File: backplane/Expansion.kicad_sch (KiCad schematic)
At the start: 19 parts, among them U401 74HC245, U402 74HC245, U403 74HC245, U404 74HC245, U405 74HC245, U406 74HC245, U407 ATF22V10C

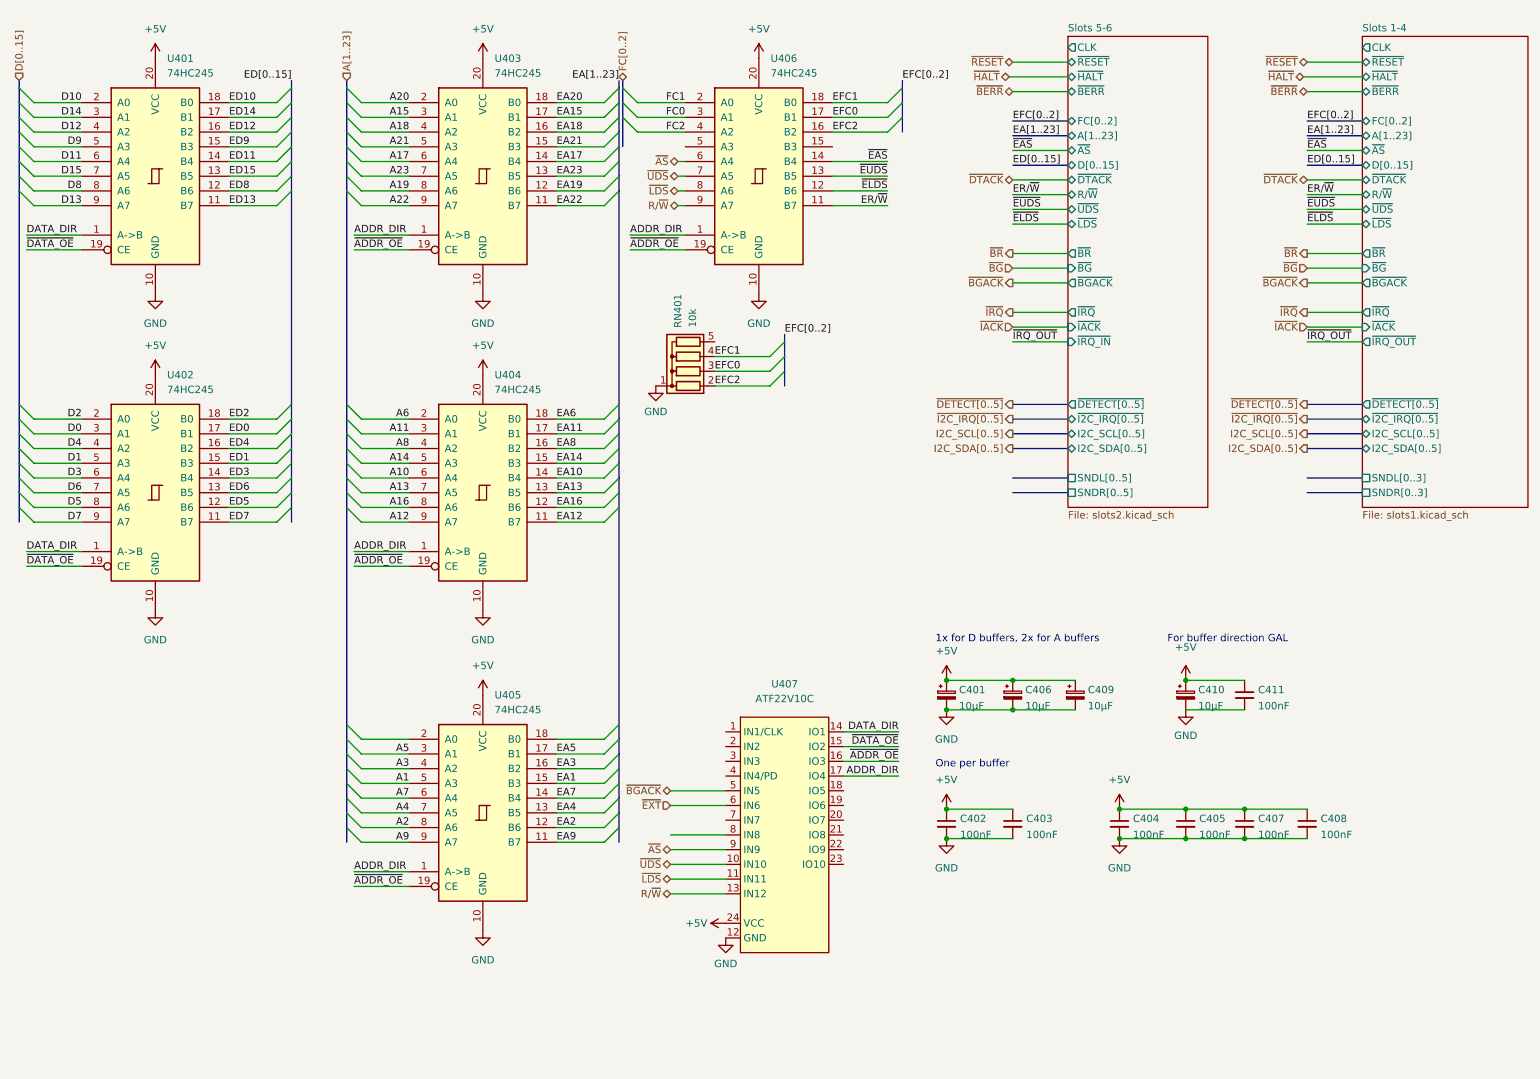
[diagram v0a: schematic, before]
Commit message: More backplane work
- Added pull up/down resistors at end of board to bring the various
  data/address lines to a controlled state, rather than floating, and
  attempt to control reflections

- Added a clock buffer so each slot gets its own nice buffered clock.

  The clock buffer used is only 1:5 fanout, so the last two slots share
  a clock line.
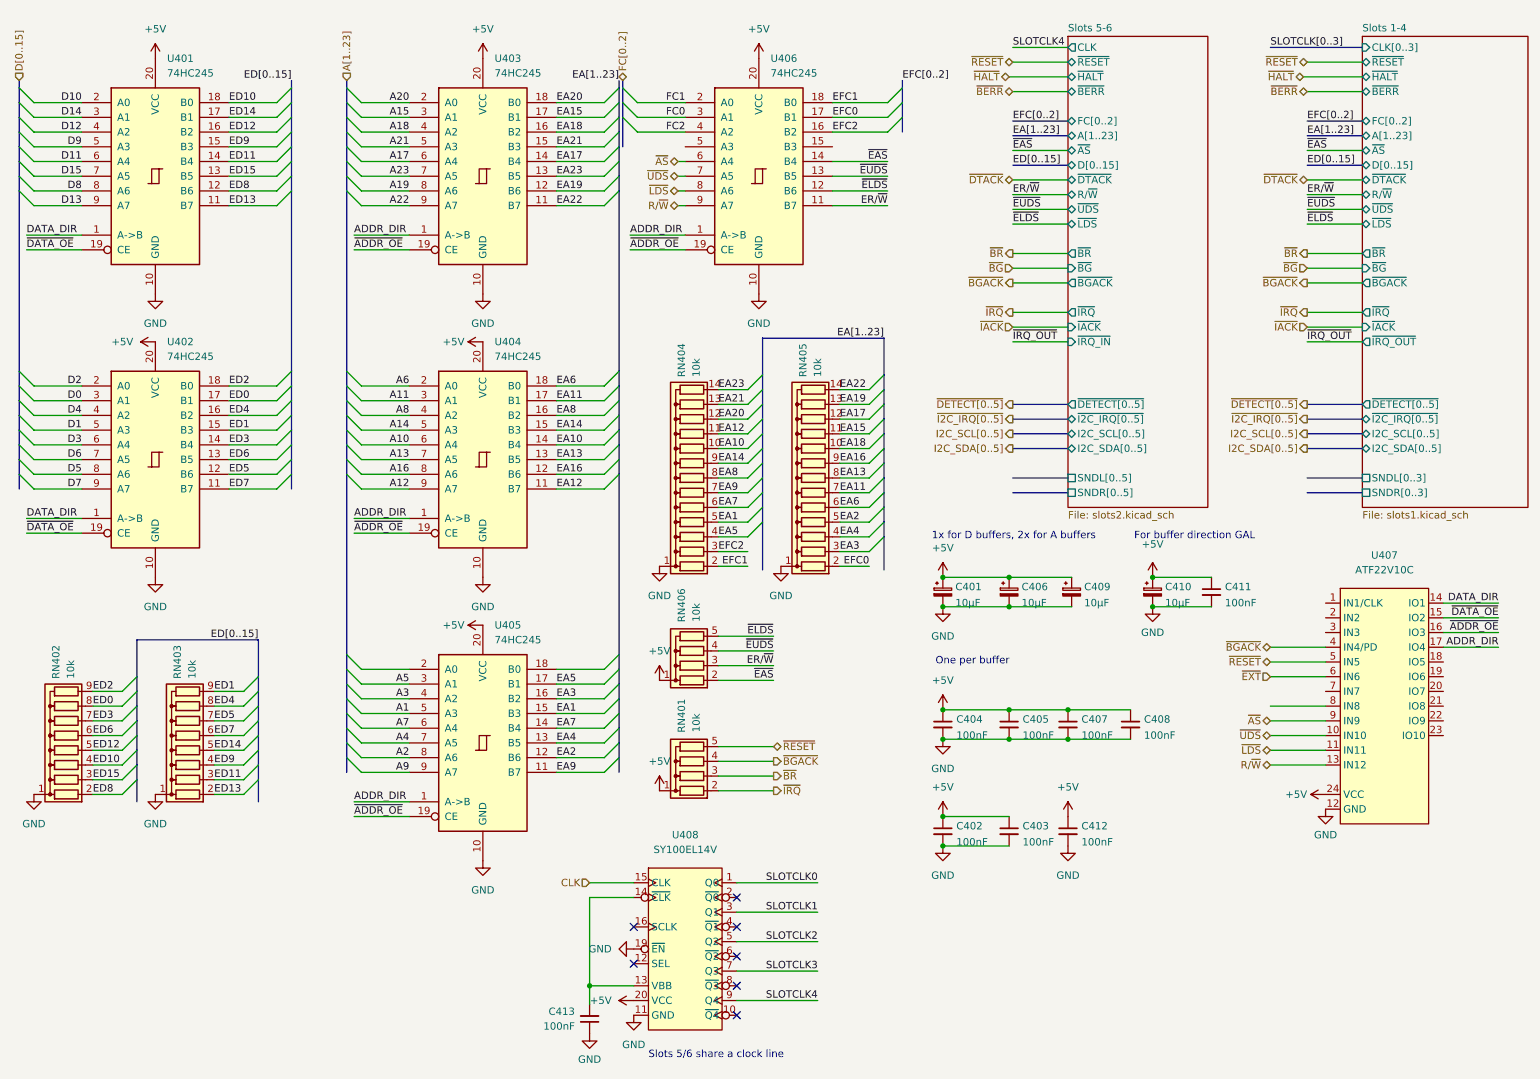
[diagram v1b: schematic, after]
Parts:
- added C412, C413: 100nF, Capacitor_SMD:C_0805_2012Metric, symbol Device:C_Small
- added RN402, RN403: 10k, Resistor_THT:R_Array_SIP9, symbol Device:R_Network08
- added RN404, RN405: 10k, Resistor_THT:R_Array_SIP14, symbol Device:R_Network13
- added RN406: 10k, Resistor_THT:R_Array_SIP5, symbol Device:R_Network04
- added U408: SY100EL14V, Package_SO:SOIC-20W_7.5x12.8mm_P1.27mm, symbol 68komputer-common:SY100EL14V
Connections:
- net +5V: now also RN401.1 (common), C412.1, RN406.1 (common), U408.18 (VCC), U408.20 (VCC)
- net EA1: now also RN404.5 (R4)
- net EA10: now also RN404.10 (R9)
- net EA11: now also RN405.7 (R6)
- net EA12: now also RN404.11 (R10)
- net EA13: now also RN405.8 (R7)
- net EA14: now also RN404.9 (R8)
- net EA15: now also RN405.11 (R10)
- net EA16: now also RN405.9 (R8)
- net EA17: now also RN405.12 (R11)
- net EA18: now also RN405.10 (R9)
- net EA19: now also RN405.13 (R12)
- net EA2: now also RN405.5 (R4)
- net EA20: now also RN404.12 (R11)
- net EA21: now also RN404.13 (R12)
- net EA22: now also RN405.14 (R13)
- net EA23: now also RN404.14 (R13)
- net EA3: now also RN405.3 (R2)
- net EA4: now also RN405.4 (R3)
- net EA5: now also RN404.4 (R3)
- net EA6: now also RN405.6 (R5)
- net EA7: now also RN404.6 (R5)
- net EA8: now also RN404.8 (R7)
- net EA9: now also RN404.7 (R6)
- net ED0: now also RN402.8 (R7)
- net ED1: now also RN403.9 (R8)
- net ED10: now also RN402.4 (R3)
- net ED11: now also RN403.3 (R2)
- net ED12: now also RN402.5 (R4)
- net ED13: now also RN403.2 (R1)
- net ED14: now also RN403.5 (R4)
- net ED15: now also RN402.3 (R2)
- net ED2: now also RN402.9 (R8)
- net ED3: now also RN402.7 (R6)
- net ED4: now also RN403.8 (R7)
- net ED5: now also RN403.7 (R6)
- net ED6: now also RN402.6 (R5)
- net ED7: now also RN403.6 (R5)
- net ED8: now also RN402.2 (R1)
- net ED9: now also RN403.4 (R3)
- net EFC0: now also RN405.2 (R1); no longer RN401.3 (R2)
- net EFC1: now also RN404.2 (R1); no longer RN401.4 (R3)
- net EFC2: now also RN404.3 (R2); no longer RN401.2 (R1)
- net ER/~{W}: now also RN406.3 (R2)
- net GND: now also C412.2, C413.1, RN402.1 (common), RN403.1 (common), RN404.1 (common), RN405.1 (common), U408.11 (GND), U408.19 (~{EN}); no longer RN401.1 (common)
- net ~{BGACK}: now also RN401.4 (R3), U407.4 (IN4/PD); no longer U407.5 (IN5)
- net ~{BR}: now also RN401.3 (R2)
- net ~{EAS}: now also RN406.2 (R1)
- net ~{ELDS}: now also RN406.5 (R4)
- net ~{EUDS}: now also RN406.4 (R3)
- net ~{IRQ}: now also RN401.2 (R1)
- net ~{RESET}: now also RN401.5 (R4), U407.5 (IN5)
- new net: C413.2, U408.13 (VBB), U408.14 (~{CLK})
- new net CLK: U408.15 (CLK)
- new net SLOTCLK0: U408.1 (Q0)
- new net SLOTCLK1: U408.3 (Q1)
- new net SLOTCLK2: U408.5 (Q2)
- new net SLOTCLK3: U408.7 (Q3)
- new net SLOTCLK4: U408.9 (Q4)
- no-connect marks 0 -> 7
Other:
- sheet Slots 1-4 ports: added CLK[0..3]; removed CLK
- note added: "Slots 5/6 share a clock line"
- moved on the sheet: C401, C402, C403, C404, C405, C406, C407, C408, C409, C410, C411, U402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

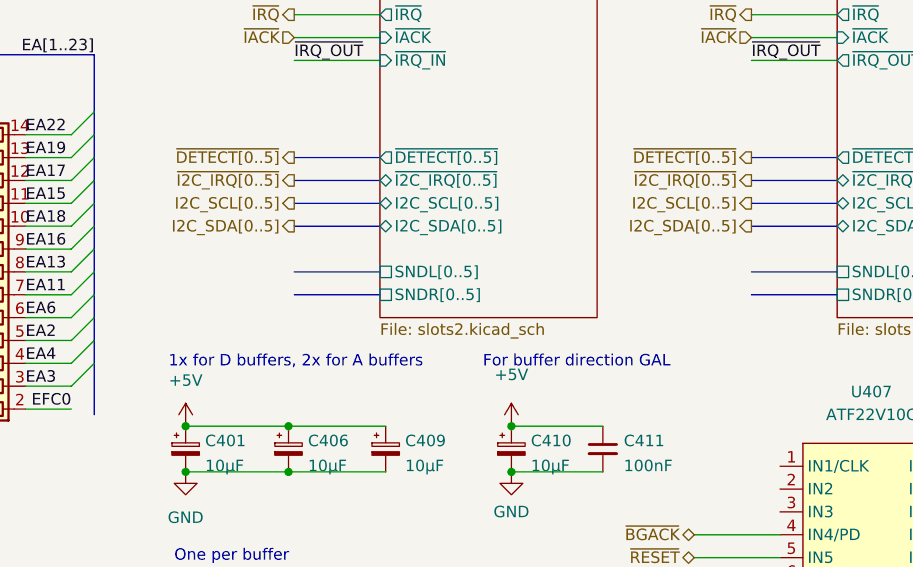
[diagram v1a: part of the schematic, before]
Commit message: Added audio mixer to backplane
- Implemented mixing (via resistors and an op amp) for the audio outputs
  from each slot and CPU card. These inputs are tied to ground through
  weak pull downs, so peripherals can leave the pins open if they're not
  being used.

  It's possible that the resistance values for the mixer aren't quite
  correct and will produce a distorted mess with many peripherals
  outputting sound simultaneously; if that's an issue, we can adjust the
  value of the resistors or add per slot trimmers to adjust each slots'
  relative volume.
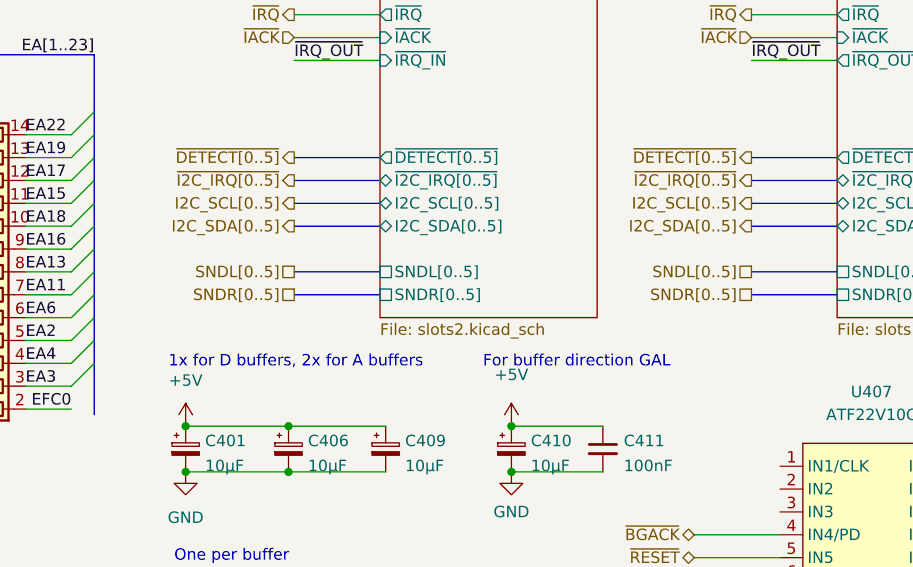
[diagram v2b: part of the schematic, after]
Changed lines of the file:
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@@
+    (effects (font (size 1.27 1.27)) (justify right))
+  )
+  (hierarchical_label "SNDR[0..5]" (shape passive) (at 241.935 97.79 180)
+    (effects (font (size 1.27 1.27)) (justify right))
+  )
+  (hierarchical_label "SNDL[0..5]" (shape passive) (at 191.135 95.25 180)
     (effects (font (size 1.27 1.27)) (justify right))
   )
@@
   )
   (hierarchical_label "~{BG}" (shape input) (at 241.935 59.055 180)
+    (effects (font (size 1.27 1.27)) (justify right))
+  )
+  (hierarchical_label "SNDL[0..5]" (shape passive) (at 241.935 95.25 180)
     (effects (font (size 1.27 1.27)) (justify right))
   )
@@
     (effects (font (size 1.27 1.27)) (justify left))
   )
+  (hierarchical_label "SNDR[0..5]" (shape passive) (at 191.135 97.79 180)
+    (effects (font (size 1.27 1.27)) (justify right))
+  )
   (hierarchical_label "~{IRQ}" (shape output) (at 191.135 66.675 180)
